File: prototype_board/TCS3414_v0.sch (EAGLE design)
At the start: 6 parts, among them U1 TCS3414FNFN

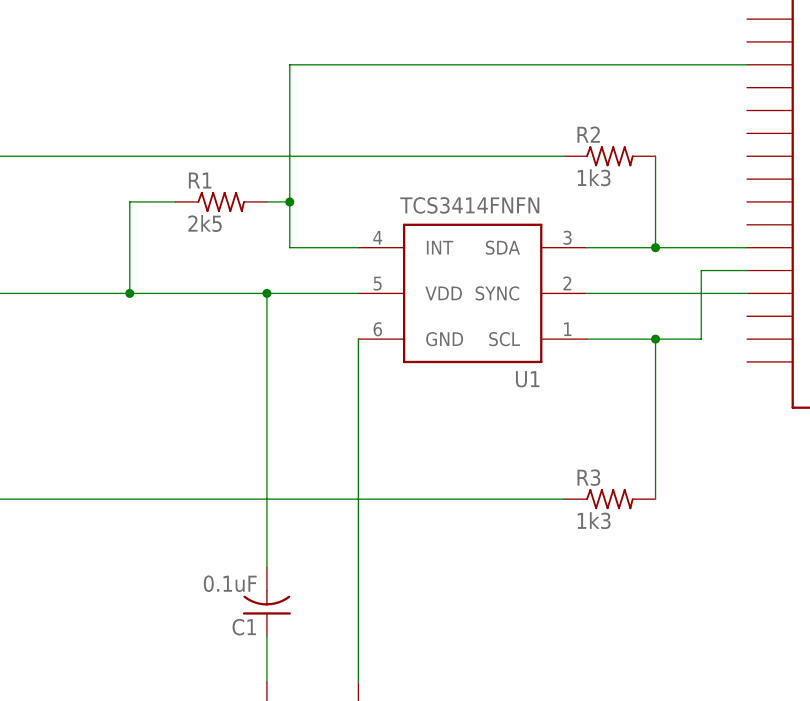
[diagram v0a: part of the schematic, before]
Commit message: Changed resistor values
2.5k to 10k and 1.3k to 4.7k resistor changes
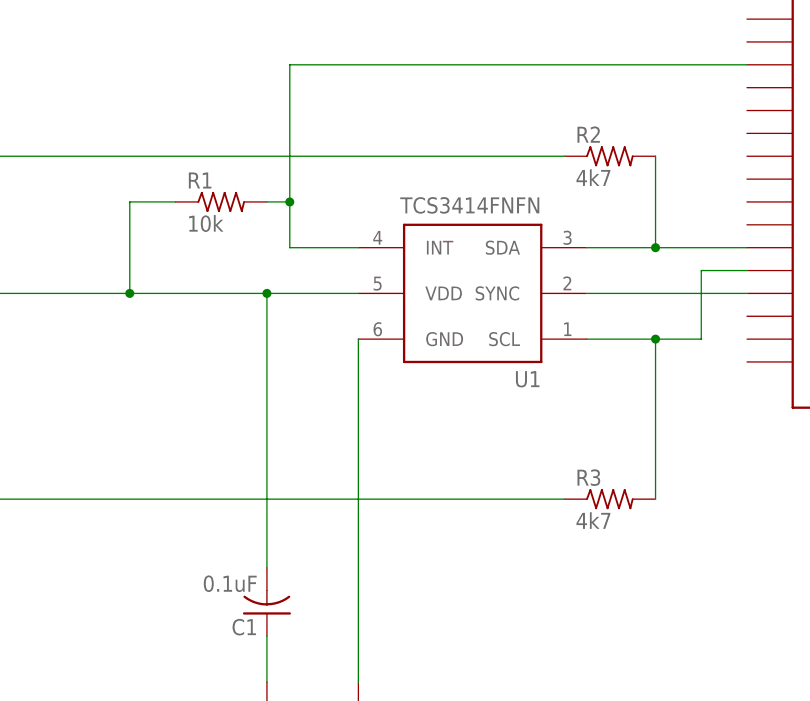
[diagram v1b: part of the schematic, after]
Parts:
- R1: value 2k5 -> 10k
- R2, R3: value 1k3 -> 4k7
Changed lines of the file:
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@@
 <?xml version="1.0" encoding="utf-8"?>
 <!DOCTYPE eagle SYSTEM "eagle.dtd">
-<eagle version="7.4.0">
+<eagle version="6.6.0">
 <drawing>
 <settings>
@@
 <part name="U$1" library="mcu-accessories" deviceset="TEENSY_3.1_BASIC" device=""/>
 <part name="C1" library="resistor" deviceset="C-US" device="C0603" value="0.1uF"/>
-<part name="R1" library="rcl" deviceset="R-US_" device="R0603" value="2k5"/>
-<part name="R2" library="rcl" deviceset="R-US_" device="R0603" value="1k3"/>
-<part name="R3" library="rcl" deviceset="R-US_" device="R0603" value="1k3"/>
+<part name="R1" library="rcl" deviceset="R-US_" device="R0603" value="10k"/>
+<part name="R2" library="rcl" deviceset="R-US_" device="R0603" value="4k7"/>
+<part name="R3" library="rcl" deviceset="R-US_" device="R0603" value="4k7"/>
 <part name="GND2" library="supply1" deviceset="GND" device=""/>
 <part name="GND3" library="supply1" deviceset="GND" device=""/>
